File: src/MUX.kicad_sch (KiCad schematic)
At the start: 20 parts, among them U10 TMUX1208RSVR, U5 PCF8574RGTR(UMW), U6 PCF8574RGTR(UMW), U7 TMUX1208RSVR, U8 TMUX1208RSVR, U9 TMUX1208RSVR

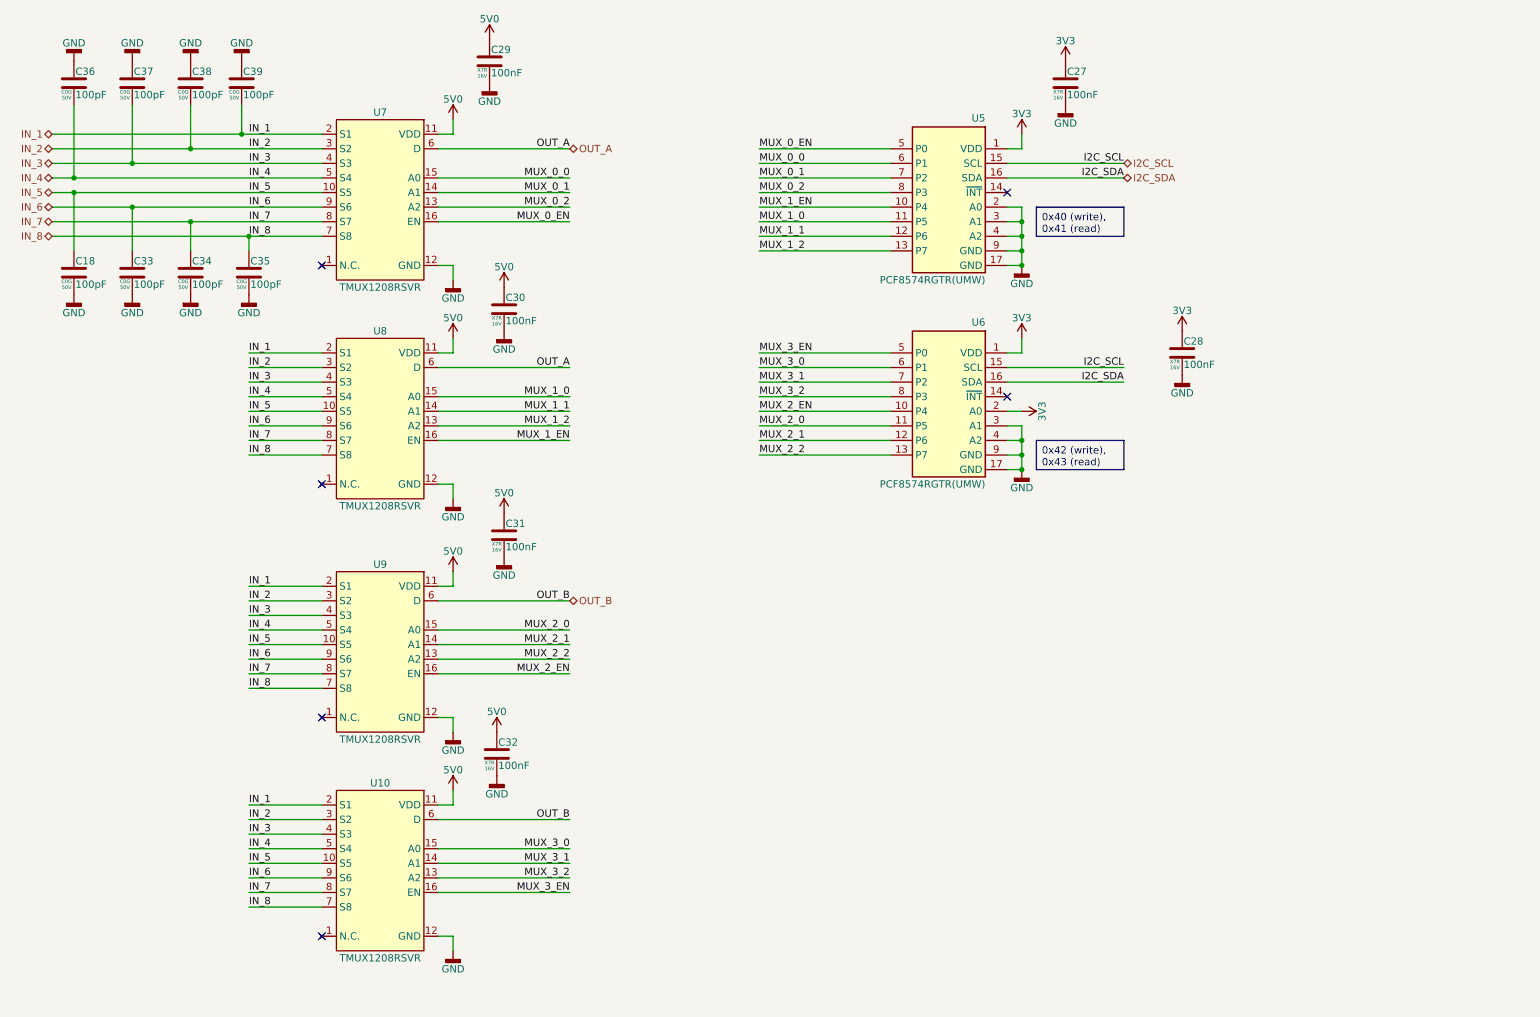
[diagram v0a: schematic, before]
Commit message: Update PCB layout and schematics; add enclosure design files
Bump firmware submodule to WAN failover scenario-audit hardening +
zombie-LTE self-heal (round 2).

Co-Authored-By: Claude Sonnet 5 <noreply@anthropic.com>
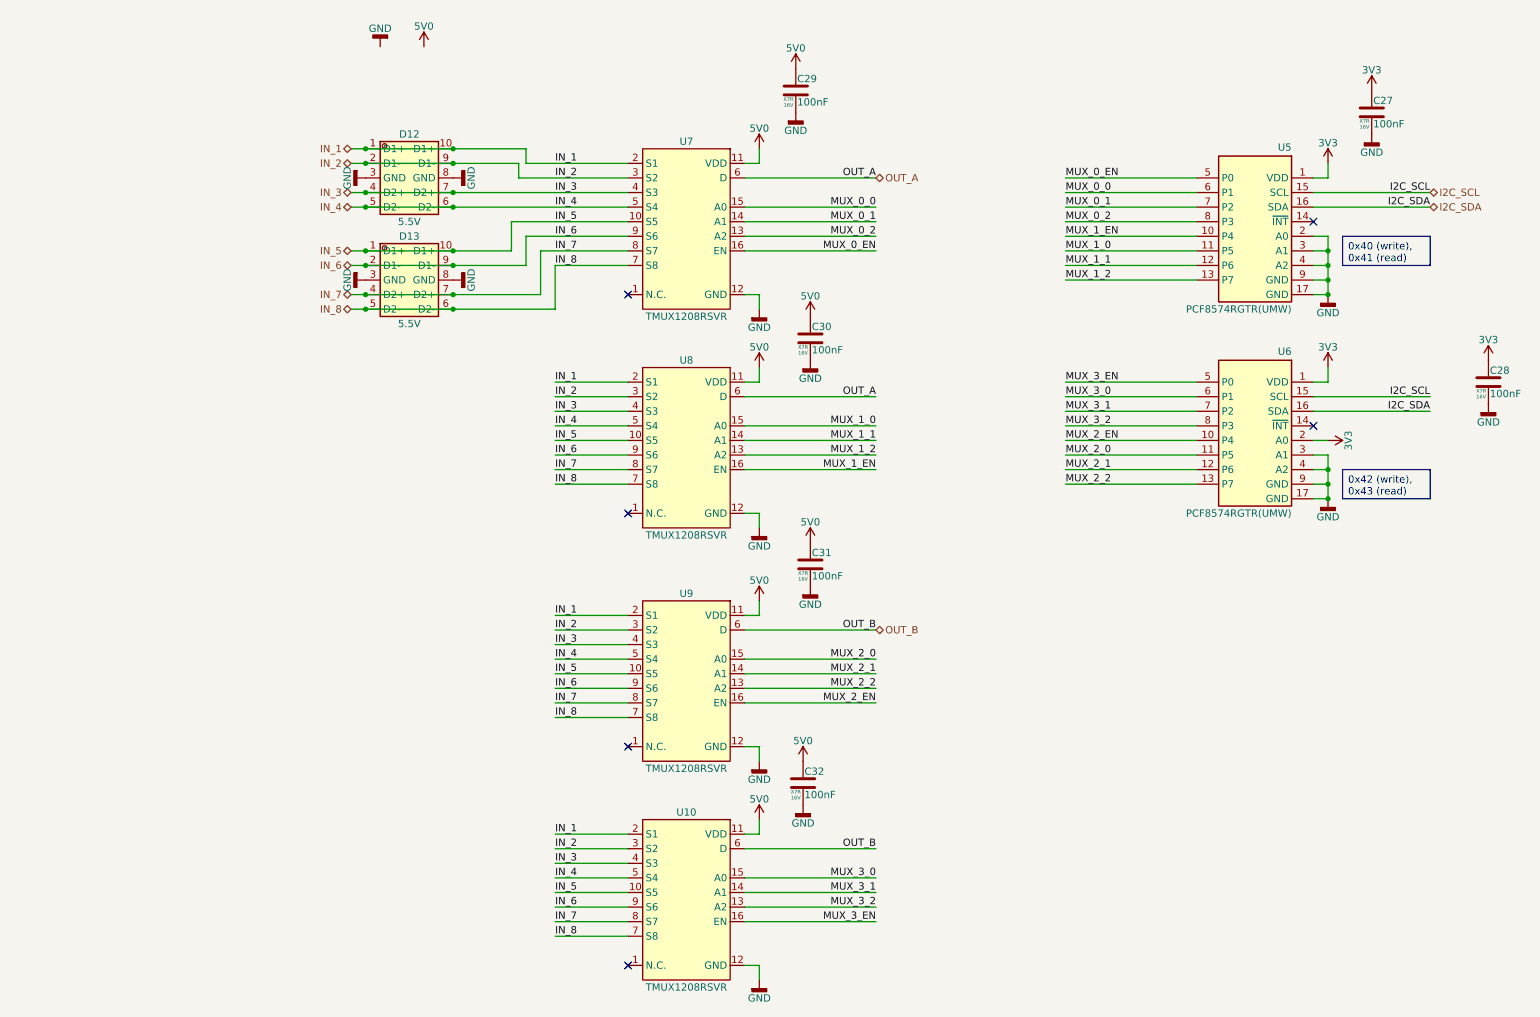
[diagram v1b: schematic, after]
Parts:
- removed C18, C33, C34, C35, C36, C37, C38, C39: 100pF, 7Sigma:C_0402_1005Metric, symbol Capacitor:0402CG101J500NT
- added D12, D13: 5.5V, 7Sigma:USON-10_2.5x1.0mm_P0.5mm, symbol Diodes:TPD4E05U06DQAR
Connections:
- net GND: now also D12.3 (GND), D12.8 (GND), D13.3 (GND), D13.8 (GND)
- net IN_1: now also D12.1 (D1+), D12.10 (D1+)
- net IN_2: now also D12.2 (D1-), D12.9 (D1-)
- net IN_3: now also D12.4 (D2+), D12.7 (D2+)
- net IN_4: now also D12.5 (D2-), D12.6 (D2-)
- net IN_5: now also D13.1 (D1+), D13.10 (D1+)
- net IN_6: now also D13.2 (D1-), D13.9 (D1-)
- net IN_7: now also D13.4 (D2+), D13.7 (D2+)
- net IN_8: now also D13.5 (D2-), D13.6 (D2-)
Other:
- moved on the sheet: C27, C28, C29, C30, C31, C32, U10, U5, U6, U7, U8, U9
